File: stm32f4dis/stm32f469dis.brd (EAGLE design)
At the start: 0 parts

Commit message: eagle v2
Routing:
- net GND: track 0.00 -> 62.7 mm, vias 0 -> 6
- net S$26: track 53.1 -> 0.00 mm, vias 3 -> 0
- net S$17: track 0.00 -> 39.7 mm, vias 0 -> 1
- net S$72: track 38.9 -> 0.00 mm, vias 2 -> 0
- net S$41: track 3.81 -> 41.7 mm, vias 1 -> 2
- net S$42: track 3.81 -> 33.9 mm, vias 1 -> 2
- net S$65: track 18.3 -> 0.00 mm, vias 1 -> 0
- net S$49: track 17.1 -> 0.00 mm, vias 1 -> 0
- net S$47: track 27.2 -> 17.8 mm, vias 1 -> 0
- net S$27: track 0.00 -> 8.98 mm, vias 0 -> 2
- net S$63: track 55.5 -> 63.9 mm
- net S$68: track 0.00 -> 4.86 mm, vias 0 -> 1
- net S$2: track 22.6 -> 18.1 mm
- net S$4: track 23.8 -> 26.1 mm
- net S$5: track 23.8 -> 26.1 mm
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
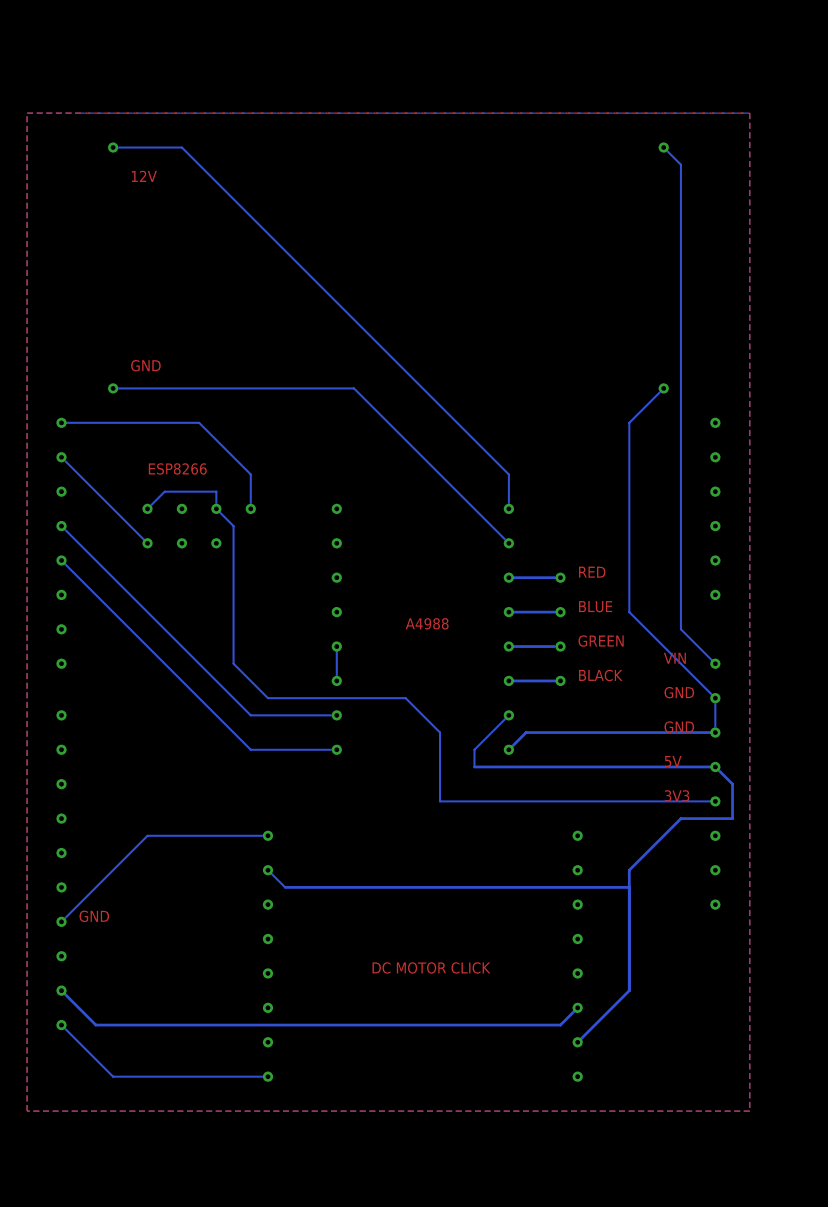
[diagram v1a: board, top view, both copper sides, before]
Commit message: change layout, drill size, route width, isolation
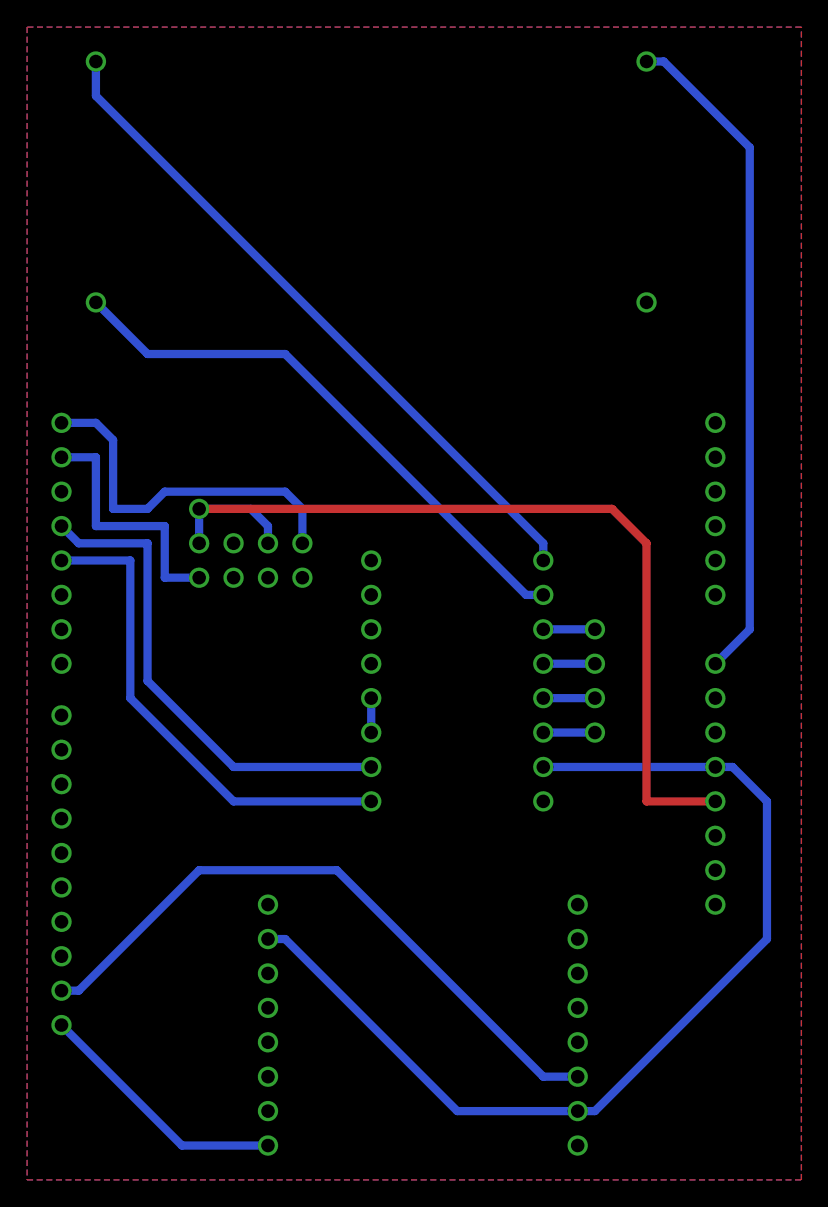
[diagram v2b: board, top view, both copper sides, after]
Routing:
- net 5V: track 0.00 -> 75.1 mm, vias 0 -> 5
- net 3V3: track 0.00 -> 67.6 mm, vias 0 -> 4
- net S$63: track 63.9 -> 0.00 mm, vias 2 -> 0
- net GND: track 62.7 -> 0.00 mm, vias 6 -> 7
- net 12V: track 0.00 -> 50.5 mm, vias 0 -> 2
- net D14: track 0.00 -> 48.1 mm, vias 0 -> 2
- net 12VGND: track 0.00 -> 42.0 mm, vias 0 -> 2
- net S$41: track 41.7 -> 0.00 mm, vias 2 -> 0
- net S$62: track 39.7 -> 0.00 mm, vias 2 -> 0
- net S$17: track 39.7 -> 0.00 mm, vias 1 -> 0
- net D3: track 0.00 -> 36.2 mm, vias 0 -> 2
- net D4: track 0.00 -> 36.2 mm, vias 0 -> 2
- net S$42: track 33.9 -> 0.00 mm, vias 2 -> 0
- net S$5: track 26.1 -> 0.00 mm, vias 2 -> 0
- net S$4: track 26.1 -> 0.00 mm, vias 2 -> 0
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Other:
- board text added: "BLK"
- board text added: "ESP"
- board text added: "GRN"
- board text removed: "BLACK"
- board text removed: "ESP8266"
- board text removed: "GREEN"

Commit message: improve layout
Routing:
- net S$2: track 13.8 -> 15.5 mm
- net 5V: track 75.1 -> 74.0 mm
- net D0: track 13.2 -> 12.5 mm
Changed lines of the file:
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@@
 <polygon width="0.6096" layer="16" isolate="0.8128">
 <vertex x="-99.06" y="85.09"/>
-<vertex x="-41.91" y="85.09"/>
-<vertex x="-41.91" y="170.18"/>
+<vertex x="-43.18" y="85.09"/>
+<vertex x="-43.18" y="170.18"/>
 <vertex x="-99.06" y="170.18"/>
 </polygon>
 <polygon width="0.6096" layer="1" isolate="0.6096">
 <vertex x="-99.06" y="85.09"/>
-<vertex x="-41.91" y="85.09"/>
-<vertex x="-41.91" y="170.18"/>
+<vertex x="-43.18" y="85.09"/>
+<vertex x="-43.18" y="170.18"/>
 <vertex x="-99.06" y="170.18"/>
 </polygon>
@@
 <via x="-48.26" y="115.57" extent="1-16" drill="1"/>
 <wire x1="-48.26" y1="115.57" x2="-46.99" y2="115.57" width="0.6096" layer="16"/>
-<wire x1="-46.99" y1="115.57" x2="-44.45" y2="113.03" width="0.6096" layer="16"/>
-<wire x1="-44.45" y1="113.03" x2="-44.45" y2="102.87" width="0.6096" layer="16"/>
-<wire x1="-44.45" y1="102.87" x2="-57.15" y2="90.17" width="0.6096" layer="16"/>
+<wire x1="-46.99" y1="115.57" x2="-45.72" y2="114.3" width="0.6096" layer="16"/>
+<wire x1="-45.72" y1="114.3" x2="-45.72" y2="101.6" width="0.6096" layer="16"/>
+<wire x1="-45.72" y1="101.6" x2="-57.15" y2="90.17" width="0.6096" layer="16"/>
 <wire x1="-57.15" y1="90.17" x2="-58.42" y2="90.17" width="0.6096" layer="16"/>
 <wire x1="-81.28" y1="102.87" x2="-80.01" y2="102.87" width="0.6096" layer="16"/>
@@
 <wire x1="-92.71" y1="139.7" x2="-92.71" y2="134.62" width="0.6096" layer="16"/>
 <wire x1="-92.71" y1="134.62" x2="-90.17" y2="134.62" width="0.6096" layer="16"/>
-<wire x1="-90.17" y1="134.62" x2="-88.9" y2="135.89" width="0.6096" layer="16"/>
+<wire x1="-90.17" y1="134.62" x2="-87.63" y2="137.16" width="0.6096" layer="16"/>
 </signal>
 <signal name="D0">
 <via x="-78.74" y="132.08" extent="1-16" drill="1"/>
 <wire x1="-78.74" y1="134.62" x2="-78.74" y2="132.08" width="0.6096" layer="16"/>
-<wire x1="-88.9" y1="135.89" x2="-80.01" y2="135.89" width="0.6096" layer="16"/>
-<wire x1="-80.01" y1="135.89" x2="-78.74" y2="134.62" width="0.6096" layer="16"/>
+<wire x1="-87.63" y1="137.16" x2="-81.28" y2="137.16" width="0.6096" layer="16"/>
+<wire x1="-81.28" y1="137.16" x2="-78.74" y2="134.62" width="0.6096" layer="16"/>
 </signal>
 <signal name="S$40">
